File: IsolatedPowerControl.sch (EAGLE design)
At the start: 42 parts, among them Q1 FDN340P, Q2 FDN340P, U1 MCP23008-E/SO, U2 MCP4716A0T-E/CH, U3 MCP6273T-E/CH

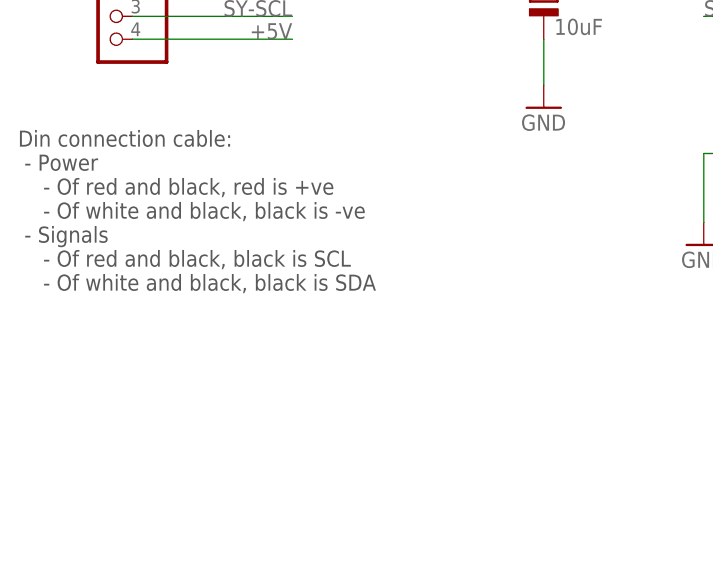
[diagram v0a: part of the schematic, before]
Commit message: Fixed an error in the cable colour note
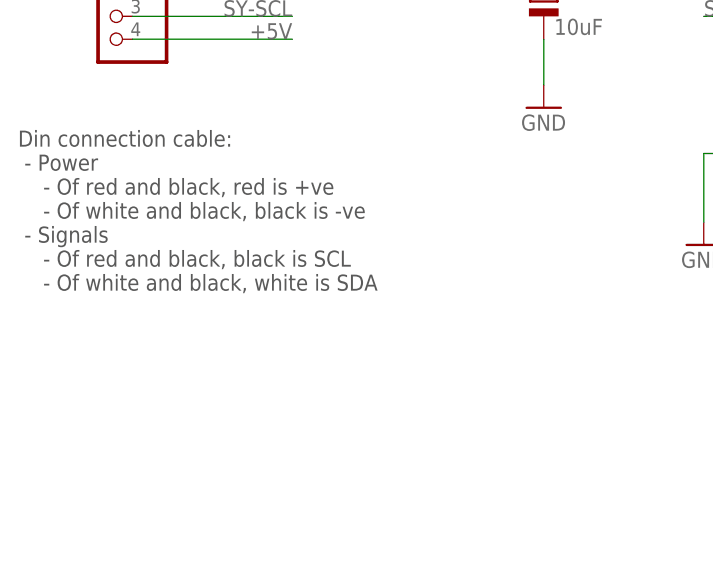
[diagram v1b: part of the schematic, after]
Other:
- note added: "Din connection cable: - Power - Of red and black, red is +ve - Of white and black, black is -ve - Signals - Of red and black, black is SCL - Of white and black, white is SDA"
- note removed: "Din connection cable: - Power - Of red and black, red is +ve - Of white and black, black is -ve - Signals - Of red and black, black is SCL - Of white and black, black is SDA"
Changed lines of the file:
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@@
  - Signals
     - Of red and black, black is SCL
-    - Of white and black, black is SDA</text>
+    - Of white and black, white is SDA</text>
 </plain>
 <instances>
